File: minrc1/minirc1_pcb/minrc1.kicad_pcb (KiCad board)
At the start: 2 copper layers, 39 x 49.5 mm, 18 parts, among them J3 Conn_01x04, J4 Conn_01x04, U1 DRV8837D, U2 DRV8837D, U3 DRV8837D, U4 DRV8837D, U5 ESP32S3

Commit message: finish turtlebot
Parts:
- added C1: 0.1uF, Resistor_SMD:R_0402_1005Metric, F.Cu at (136.7, 106.3)
- added C10: 0.1uF, Resistor_SMD:R_0402_1005Metric, F.Cu at (163.3, 113.2)
- added C11: 0.1uF, Resistor_SMD:R_0402_1005Metric, F.Cu at (138.3, 102.6)
- added C12: 0.1uF, Resistor_SMD:R_0402_1005Metric, F.Cu at (163.5, 103.0)
- added C13: 0.1uF, Resistor_SMD:R_0402_1005Metric, F.Cu at (155.8, 129.9)
- added C2: 0.1uF, Resistor_SMD:R_0402_1005Metric, F.Cu at (136.7, 111.8)
- added C3: 0.1uF, Resistor_SMD:R_0402_1005Metric, F.Cu at (136.7, 104.4)
- added C4: 0.1uF, Resistor_SMD:R_0402_1005Metric, F.Cu at (136.7, 109.9)
- added C5: 0.1uF, Resistor_SMD:R_0402_1005Metric, F.Cu at (161.1, 120.3)
- added C6: 10uF, Resistor_SMD:R_0402_1005Metric, F.Cu at (161.0, 103.0)
- added C7: 0.1uF, Resistor_SMD:R_0402_1005Metric, F.Cu at (163.3, 110.0)
- added C8: 0.1uF, Resistor_SMD:R_0402_1005Metric, F.Cu at (163.3, 115.1)
- added C9: 0.1uF, Resistor_SMD:R_0402_1005Metric, F.Cu at (163.3, 108.1)
- added J4: Switch, Connector_PinHeader_2.54mm:PinHeader_1x02_P2.54mm_Vertical, B.Cu at (150.0, 96.9)
- moved U5 7.48 mm to (161.5, 114.2), turned to -90 degrees
- moved U4 7.30 mm to (161.5, 109.1)
- moved U2 5.84 mm to (138.5, 111.0), turned to 90 degrees
- moved U1 2.89 mm to (138.5, 105.6), turned to 90 degrees
- moved J2 2.07 mm to (165.0, 110.0)
- moved H3 2.06 mm to (138.0, 133.5)
- moved J1 2.06 mm to (135.0, 110.0)
- moved BZ1 2.00 mm to (150.0, 127.0)
- moved H1 2.00 mm to (133.5, 103.5)
- moved H2 2.00 mm to (166.5, 103.5)
- moved H4 2.00 mm to (162.0, 133.5)
- moved MK1 2.00 mm to (137.5, 100.5), turned to -90 degrees
- moved MK2 2.00 mm to (162.5, 100.5), turned to 90 degrees
- moved MK3 2.00 mm to (150.0, 134.0)
- moved U3 2.00 mm to (150.0, 100.0)
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- renumbered J3 to J1, J4 to J2, U5 to U3, U3 to U4, U4 to U5
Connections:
- J2 pad 1: Net-(J4-Pin_1) -> Net-(J2-Pin_1)
- J2 pad 2: Net-(J4-Pin_2) -> Net-(J2-Pin_2)
- J2 pad 3: Net-(J4-Pin_3) -> Net-(J2-Pin_3)
- J2 pad 4: Net-(J4-Pin_4) -> Net-(J2-Pin_4)
- U3 pad 1: Net-(U1-IN1) -> /mic_data1
- U3 pad 11: Net-(U4-IN2) -> Net-(U3-GPIO9)
- U3 pad 12: Net-(U4-IN1) -> Net-(U3-GPIO10)
- U3 pad 13: Net-(U3-IN2) -> Net-(U3-GPIO11)
- U3 pad 14: Net-(U3-IN1) -> Net-(U3-GPIO12)
- U3 pad 2: Net-(U1-IN2) -> Net-(U1-IN1)
- U3 pad 3: Net-(U2-IN1) -> Net-(U1-IN2)
- U3 pad 4: Net-(U2-IN2) -> Net-(U2-IN1)
- U3 pad 5: Net-(BZ1--) -> Net-(U2-IN2)
- U3 pad 6: Net-(BZ1-+) -> /mic_data3
- U3 pad 7: /mic_data1 -> /mic_clk
- U3 pad 8: /mic_data3 -> Net-(BZ1--)
- U3 pad 9: /mic_clk -> Net-(BZ1-+)
- U4 pad 2: Net-(J4-Pin_1) -> Net-(J2-Pin_3)
- U4 pad 3: Net-(J4-Pin_2) -> Net-(J2-Pin_4)
- U4 pad 5: Net-(U3-IN2) -> Net-(U3-GPIO12)
- U4 pad 6: Net-(U3-IN1) -> Net-(U3-GPIO11)
- U5 pad 2: Net-(J4-Pin_3) -> Net-(J2-Pin_1)
- U5 pad 3: Net-(J4-Pin_4) -> Net-(J2-Pin_2)
- U5 pad 5: Net-(U4-IN2) -> Net-(U3-GPIO10)
- U5 pad 6: Net-(U4-IN1) -> Net-(U3-GPIO9)
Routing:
- net +3.3V: track 0.00 -> 113.0 mm, vias 0 -> 8
- net /mic_clk: track 0.00 -> 81.5 mm, vias 0 -> 1
- net VBUS: track 0.00 -> 69.7 mm, vias 0 -> 4
- net /mic_data3: track 0.00 -> 26.7 mm
- net Net-(BZ1-+): track 0.00 -> 14.7 mm
- net Net-(BZ1--): track 0.00 -> 13.8 mm
- net /BATT+: track 0.00 -> 11.9 mm, vias 0 -> 1
- net /mic_data2: track 0.00 -> 9.94 mm, vias 0 -> 2
- net Net-(J1-Pin_4): track 0.00 -> 5.97 mm
- net Net-(J1-Pin_3): track 0.00 -> 5.83 mm
- net Net-(J2-Pin_3): track 0.00 -> 5.77 mm
- net Net-(U3-GPIO8): track 0.00 -> 5.58 mm
- net Net-(J2-Pin_4): track 0.00 -> 5.50 mm
- net Net-(J2-Pin_2): track 0.00 -> 4.98 mm
- net Net-(U3-GPIO11): track 0.00 -> 4.88 mm
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- added copper zone on B.Cu, net GND
- added copper zone on F.Cu, net GND
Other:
- board size 39 x 49.5 mm -> 39.6 x 49.1 mm
- board text added: "1"
- board text added: "10"
- board text added: "11"
- board text added: "12"
- board text added: "2"
- board text added: "3"
- board text added: "44"
- board text added: "9"
- board text added: "IO6"
- board text added: "IO7"
- board text added: "OFF"
- board text added: "ON"
- board text added: "bat+"
- board text added: "by Chris Xu"
- board text added: "chrg"
- board text added: "minirc1"

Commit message: update readme
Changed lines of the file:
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@@
 	)
 	(segment
-		(start 137.3 104.55)
-		(end 138.25 103.6)
+		(start 137.3 104.4)
+		(end 138.1 103.6)
 		(width 0.4)
 		(layer "B.Cu")
@@
 	)
 	(segment
+		(start 138.1 103.6)
+		(end 138.25 103.6)
+		(width 0.4)
+		(layer "B.Cu")
+		(net "+3.3V")
+	)
+	(segment
 		(start 157.62 105.08)
 		(end 158.518144 105.08)
@@
 	)
 	(segment
-		(start 137.3 106.8)
-		(end 137.3 104.55)
-		(width 0.4)
-		(layer "B.Cu")
-		(net "+3.3V")
-	)
-	(segment
 		(start 160.03 121.13)
 		(end 160.033879 121.133879)
@@
 	)
 	(segment
+		(start 137.3 106.8)
+		(end 137.3 104.4)
+		(width 0.4)
+		(layer "B.Cu")
+		(net "+3.3V")
+	)
+	(segment
 		(start 155.5 122.9)
 		(end 158.40918 122.9)
@@
 	)
 	(segment
-		(start 136.91 103.89)
-		(end 136.7 103.89)
-		(width 0.2)
-		(layer "F.Cu")
-		(net "VBUS")
-	)
-	(segment
 		(start 137.46 104.65)
 		(end 136.7 103.89)
@@
 	(segment
 		(start 137 103.3)
-		(end 136.91 103.89)
+		(end 136.7 103.6)
 		(width 0.2)
 		(layer "F.Cu")
@@
 	)
 	(segment
+		(start 136.7 103.6)
+		(end 136.7 103.89)
+		(width 0.2)
+		(layer "F.Cu")
+		(net "VBUS")
+	)
+	(segment
 		(start 137.09 109.39)
 		(end 137.75 110.05)
@@
 	)
 	(segment
+		(start 136.55 107.45)
+		(end 136.55 103.75)
+		(width 0.4)
+		(layer "B.Cu")
+		(net "VBUS")
+	)
+	(segment
 		(start 163.9 107.5)
 		(end 163.9 113.1)
@@
 	)
 	(segment
-		(start 136.55 107.45)
-		(end 136.55 103.75)
-		(width 0.4)
-		(layer "B.Cu")
-		(net "VBUS")
-	)
-	(segment
 		(start 157.3 99.68)
 		(end 157.62 100)
@@
 	)
 	(segment
+		(start 138 108.9)
+		(end 136.55 107.45)
+		(width 0.4)
+		(layer "B.Cu")
+		(net "VBUS")
+	)
+	(segment
 		(start 163.874265 107.474265)
 		(end 163.9 107.5)
@@
 		(width 0.4)
 		(layer "B.Cu")
-		(net "VBUS")
-	)
-	(segment
-		(start 138 108.9)
-		(end 136.55 107.45)
-		(width 0.4)
-		(layer "B.Cu")

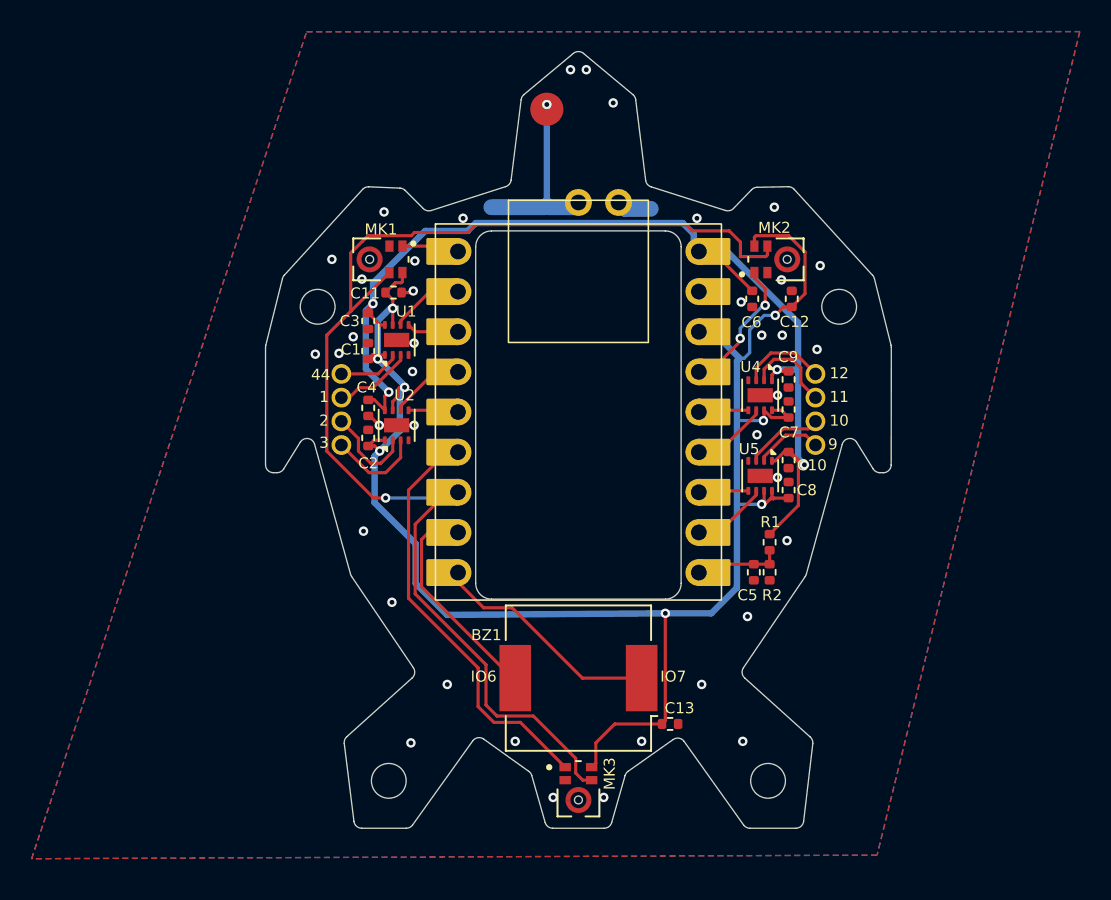
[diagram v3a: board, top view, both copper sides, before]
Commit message: stepper gui and audio
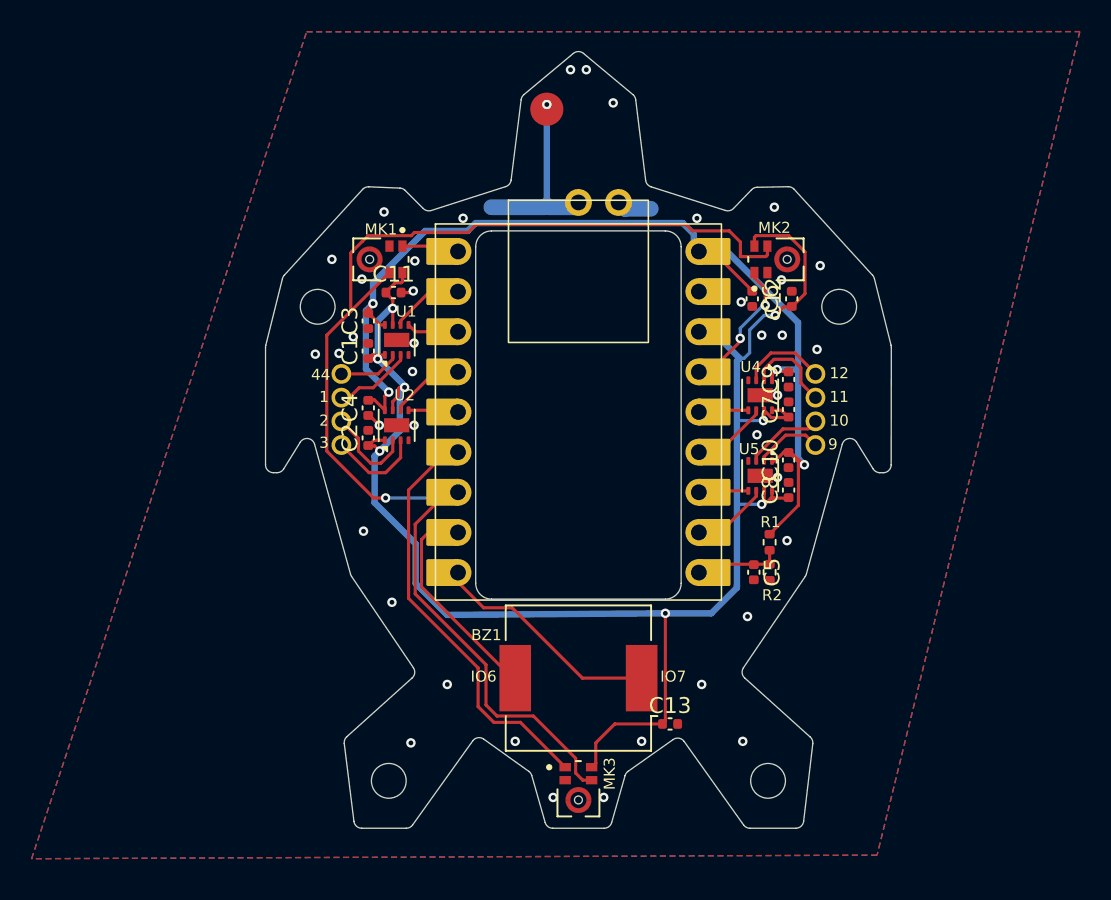
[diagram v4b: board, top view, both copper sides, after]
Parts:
- removed REF**: 3.7V_220mah_lipo_battery, minirc1:3.7V_220mah_lipo_battery
- C1, C10, C11, C12, C13, C2, C3, C4, C5, C6, C7, C8, C9: footprint Resistor_SMD:R_0402_1005Metric -> Capacitor_SMD:C_0402_1005Metric
